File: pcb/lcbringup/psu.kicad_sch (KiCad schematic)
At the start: 34 parts, among them J8 CONN_IBC_MGMT, J9 CONN_ATX12V, U10 MUN12AD03-SE, U11 MUN12AD03-SE, U5 MUN12AD03-SE, U9 MUN12AD03-SE

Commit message: Continued lcbringup layout
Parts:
- added J23: CONN_IBC_MGMT_HOST, azonenberg_pcb:CONN_MOLEX_PICOBLADE_5POS_0532610571, symbol power-azonenberg:CONN_IBC_MGMT_HOST
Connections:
- net 12V0_EN: now also J23.5 (12V0_OUT_EN)
- net 3V3_SB: now also J23.1 (3V3_SB)
- net GND: now also J23.2 (GND)
- net SUPER_I2C_SCL: now also J23.4 (I2C_SCL)
- net SUPER_I2C_SDA: now also J23.3 (I2C_SDA)
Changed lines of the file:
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@@
 	(title_block
 		(title "Andrew D. Zonenberg")
-		(date "2025-01-10")
+		(date "2025-01-14")
 		(rev "0.1")
 		(company "Antikernel Labs")
@@
 	)
 	(junction
+		(at 73.66 35.56)
+		(diameter 0)
+		(color 0 0 0 0)
+	)
+	(junction
 		(at 82.55 87.63)
 		(diameter 0)
@@
 		(pts
 			(xy 69.85 194.31) (xy 82.55 194.31)
+		)
+		(stroke
+			(width 0)
+			(type default)
+		)
+	)
+	(wire
+		(pts
+			(xy 73.66 35.56) (xy 97.79 35.56)
 		)
 		(stroke
@@
 		)
 	)
+	(label "GND"
+		(at 97.79 27.94 180)
+		(fields_autoplaced yes)
+		(effects
+			(font
+				(size 1.27 1.27)
+			)
+			(justify right bottom)
+		)
+	)
 	(label "12V0"
 		(at 50.8 204.47 180)
@@
 		)
 	)
+	(label "3V3_SB"
+		(at 97.79 25.4 180)
+		(fields_autoplaced yes)
+		(effects
+			(font
+				(size 1.27 1.27)
+			)
+			(justify right bottom)
+		)
+	)
 	(label "12V0"
 		(at 35.56 152.4 180)
@@
 		)
 	)
+	(label "SUPER_I2C_SDA"
+		(at 97.79 30.48 180)
+		(fields_autoplaced yes)
+		(effects
+			(font
+				(size 1.27 1.27)
+			)
+			(justify right bottom)
+		)
+	)
 	(label "12V0"
 		(at 35.56 114.3 180)
@@
 	(label "GND"
 		(at 80.01 170.18 180)
+		(fields_autoplaced yes)
+		(effects
+			(font
+				(size 1.27 1.27)
+			)
+			(justify right bottom)
+		)
+	)
+	(label "SUPER_I2C_SCL"
+		(at 97.79 33.02 180)
 		(fields_autoplaced yes)
 		(effects
@@
 					(unit 1)
 				)
+			)
+		)
+	)
+	(symbol
+		(lib_id "power-azonenberg:CONN_IBC_MGMT_HOST")
+		(at 101.6 36.83 0)
+		(mirror y)
+		(unit 1)
+		(exclude_from_sim no)
+		(in_bom yes)
+		(on_board yes)
+		(dnp no)
+		(fields_autoplaced yes)
+		(property "Reference" "J23"
+			(at 116.2812 29.2678 0)
+			(effects
+				(font
+					(size 1.27 1.27)
+				)
+				(justify right)
+			)
+		)
+		(property "Value" "CONN_IBC_MGMT_HOST"
+			(at 116.2812 31.6921 0)
+			(effects
+				(font
+					(size 1.27 1.27)
+				)
+				(justify right)
+			)
+		)
+		(property "Footprint" "azonenberg_pcb:CONN_MOLEX_PICOBLADE_5POS_0532610571"
+			(at 101.6 38.1 0)
+			(effects
+				(font
+					(size 1.27 1.27)
+				)
+				(hide yes)
+			)
+		)
+		(property "Datasheet" ""
+			(at 101.6 38.1 0)
+			(effects
+				(font
+					(size 1.27 1.27)
+				)
+				(hide yes)
+			)
+		)
+		(property "Description" ""
+			(at 101.6 36.83 0)
+			(effects
+				(font
+					(size 1.27 1.27)
+				)
+				(hide yes)
+			)
+		)
+		(pin "1"
+		)
+		(pin "3"
+		)
+		(pin "4"
+		)
+		(pin "5"
+		)
+		(pin "2"
+		)
+		(instances
+			(project ""
+				(path "/b833694e-84ba-499b-b91b-2564c6d12291/22a76215-e9a1-44fc-852c-4dca56c582e3"
+					(reference "J23")
+					(unit 1)
+				)

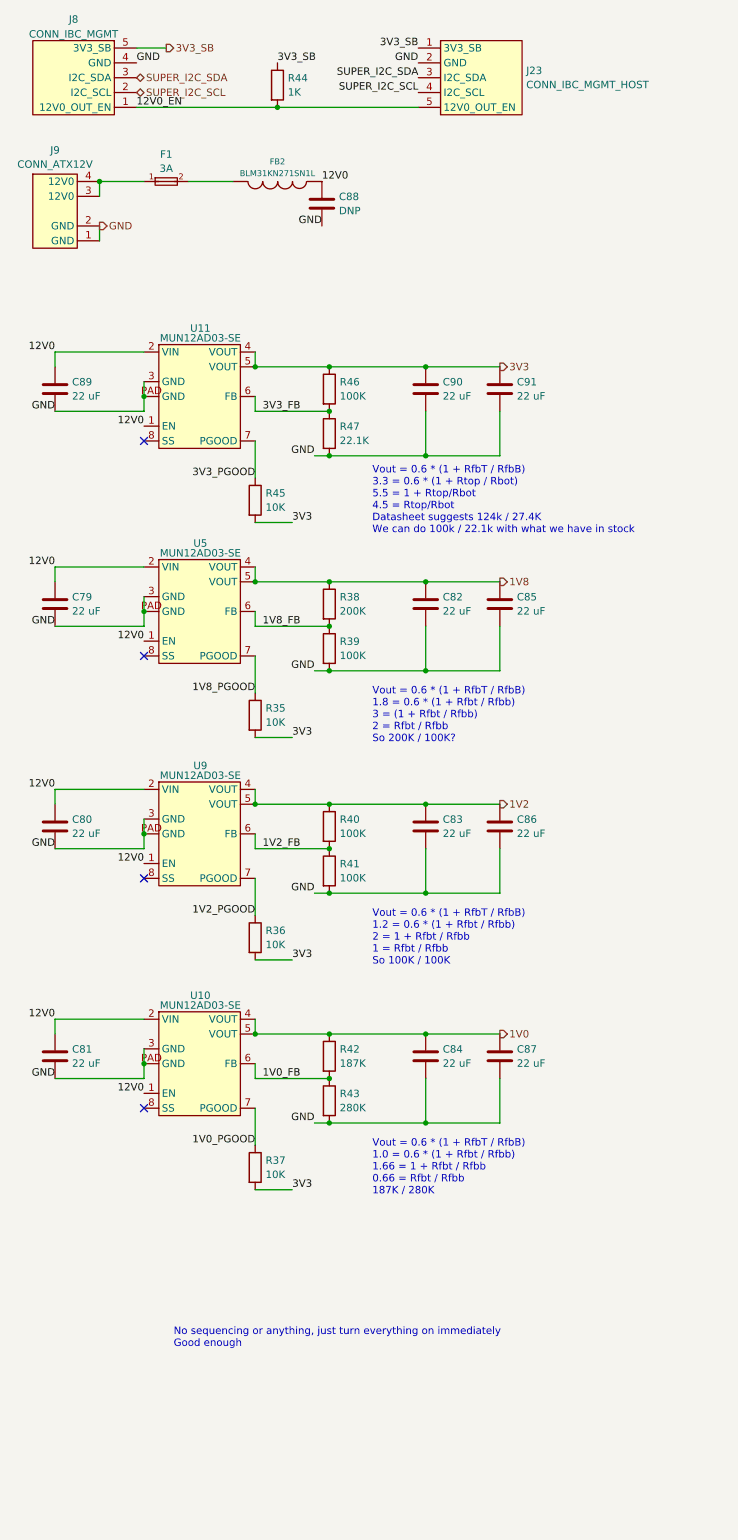
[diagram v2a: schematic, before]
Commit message: Conitnued lcbringup layout, power supply is now floorplanned
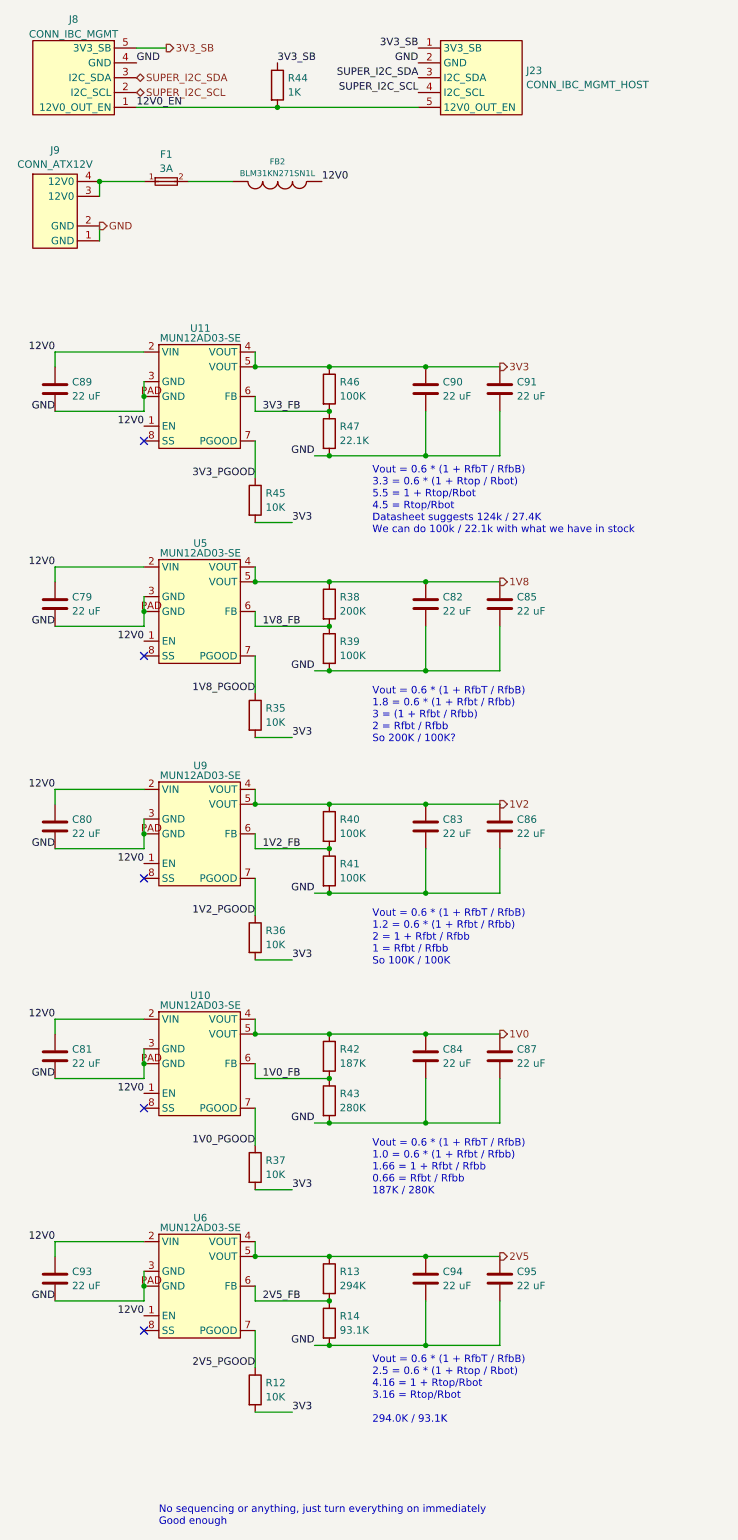
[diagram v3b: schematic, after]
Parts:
- removed C88: DNP, azonenberg_pcb:CAP_AL_10MM_SMT, symbol device:C
- added C93: 22 uF, azonenberg_pcb:EIA_1812_CAP_NOSILK, symbol device:C
- added C94, C95: 22 uF, azonenberg_pcb:EIA_1210_CAP_NOSILK, symbol device:C
- added R12: 10K, azonenberg_pcb:EIA_0402_RES_NOSILK, symbol device:R
- added R13: 294K, azonenberg_pcb:EIA_0402_RES_NOSILK, symbol device:R
- added R14: 93.1K, azonenberg_pcb:EIA_0402_RES_NOSILK, symbol device:R
- added U6: MUN12AD03-SE, azonenberg_pcb:MODULE_CYNTEC_MUN12AD03-SE, symbol power-azonenberg:MUN12AD03-SE
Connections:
- net 12V0: now also C93.1, U6.1 (EN), U6.2 (VIN)
- net 3V3: now also R12.2
- net GND: now also C93.2, C94.2, C95.2, R14.2, U6.3 (GND), U6.PAD (GND)
- new net 2V5: C94.1, C95.1, R13.1, U6.4 (VOUT), U6.5 (VOUT)
- new net 2V5_FB: R13.2, R14.1, U6.6 (FB)
- new net 2V5_PGOOD: R12.1, U6.7 (PGOOD)
- no-connect marks 4 -> 5
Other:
- note added: "Vout = 0.6 * (1 + RfbT / RfbB) 2.5 = 0.6 * (1 + Rtop / Rbot) 4.16 = 1 + Rtop/Rbot 3.16 = Rtop/Rbot 294.0K / 93.1K"

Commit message: Finished lcbringup, ready to order
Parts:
- F1: value 3A -> 1A
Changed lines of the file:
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@@
 	(title_block
 		(title "Andrew D. Zonenberg")
-		(date "2025-01-19")
+		(date "2025-01-20")
 		(rev "0.1")
 		(company "Antikernel Labs")
@@
 			)
 		)
-		(property "Value" "3A"
+		(property "Value" "1A"
 			(at 54.61 46.0318 0)
 			(effects
